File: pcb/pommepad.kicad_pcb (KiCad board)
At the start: 2 copper layers, 74.9 x 67.7 mm, 27 parts, among them SW1 SW_Push, SW2 SW_Push, SW3 SW_Push, SW4 SW_Push, SW5 SW_Push, SW6 SW_Push, U1 XIAO-RP2040-DIP, U2 OLED_0.91_128x32

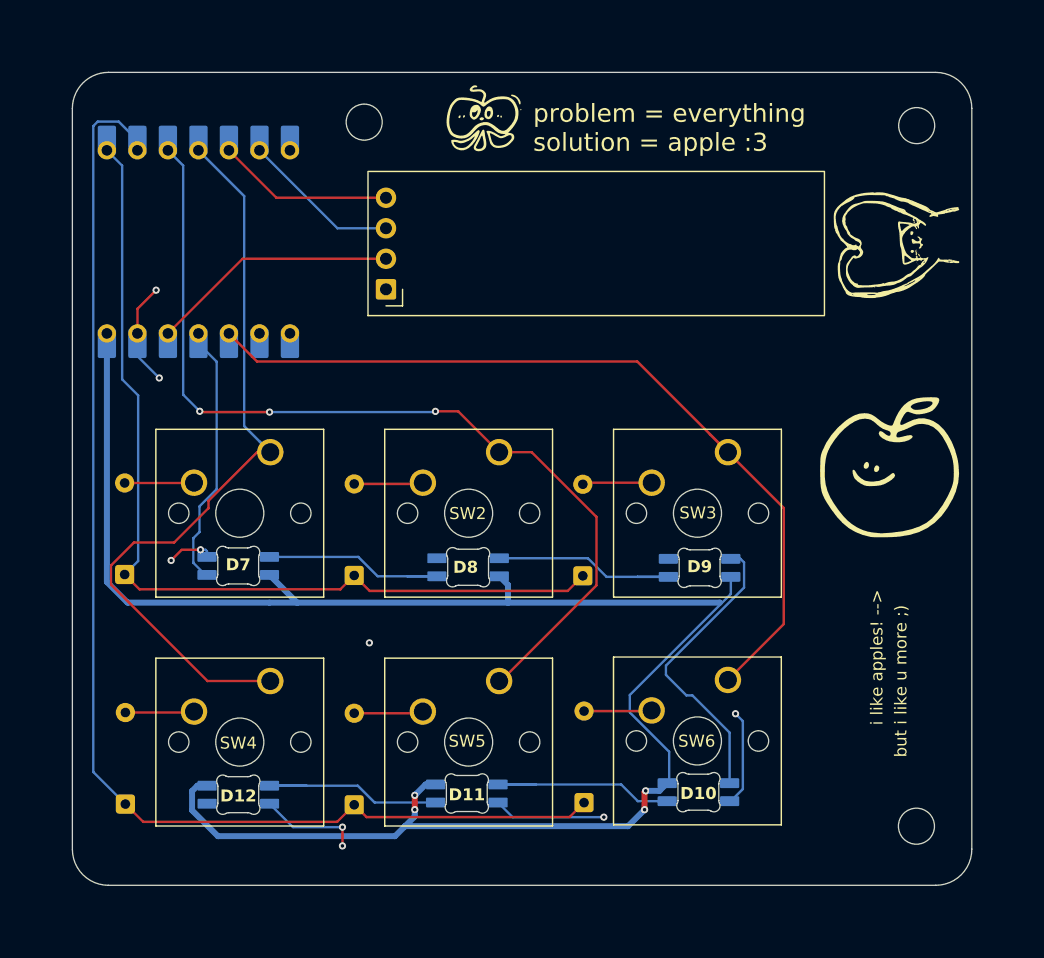
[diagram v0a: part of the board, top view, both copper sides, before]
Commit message: changing some things
changed board outline to square for easier time doing CAD, filet lines, shuffled some silkscreen around, no major changes
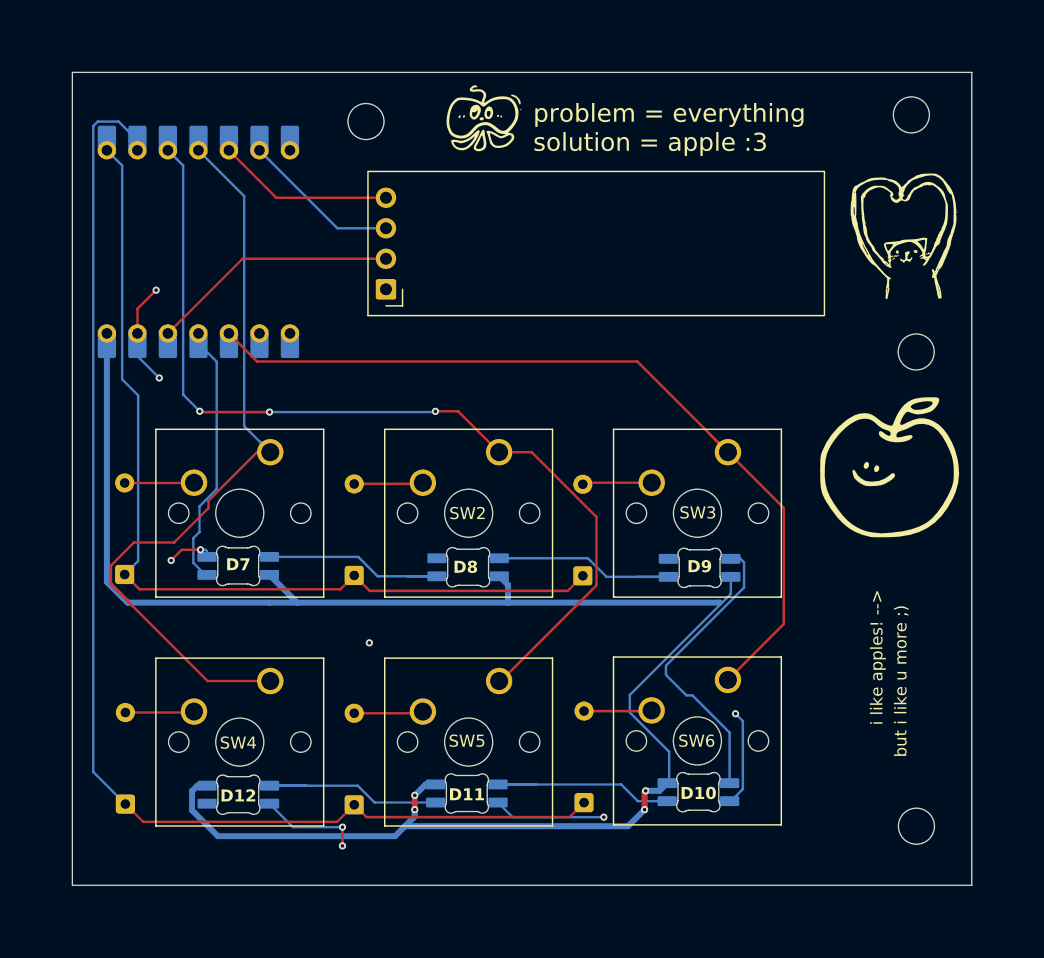
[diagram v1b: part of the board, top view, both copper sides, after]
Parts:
- added REF**: MountingHole_3mm, MountingHole:MountingHole_3mm, F.Cu at (179.9, 76.8)
- moved G*** 5.56 mm to (178.8, 63.9), turned to 0 degrees
- moved REF** 0.99 mm to (179.5, 57.1)
- moved REF** 0.16 mm to (134.1, 57.6)
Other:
- outline, holes or cut-outs redrawn

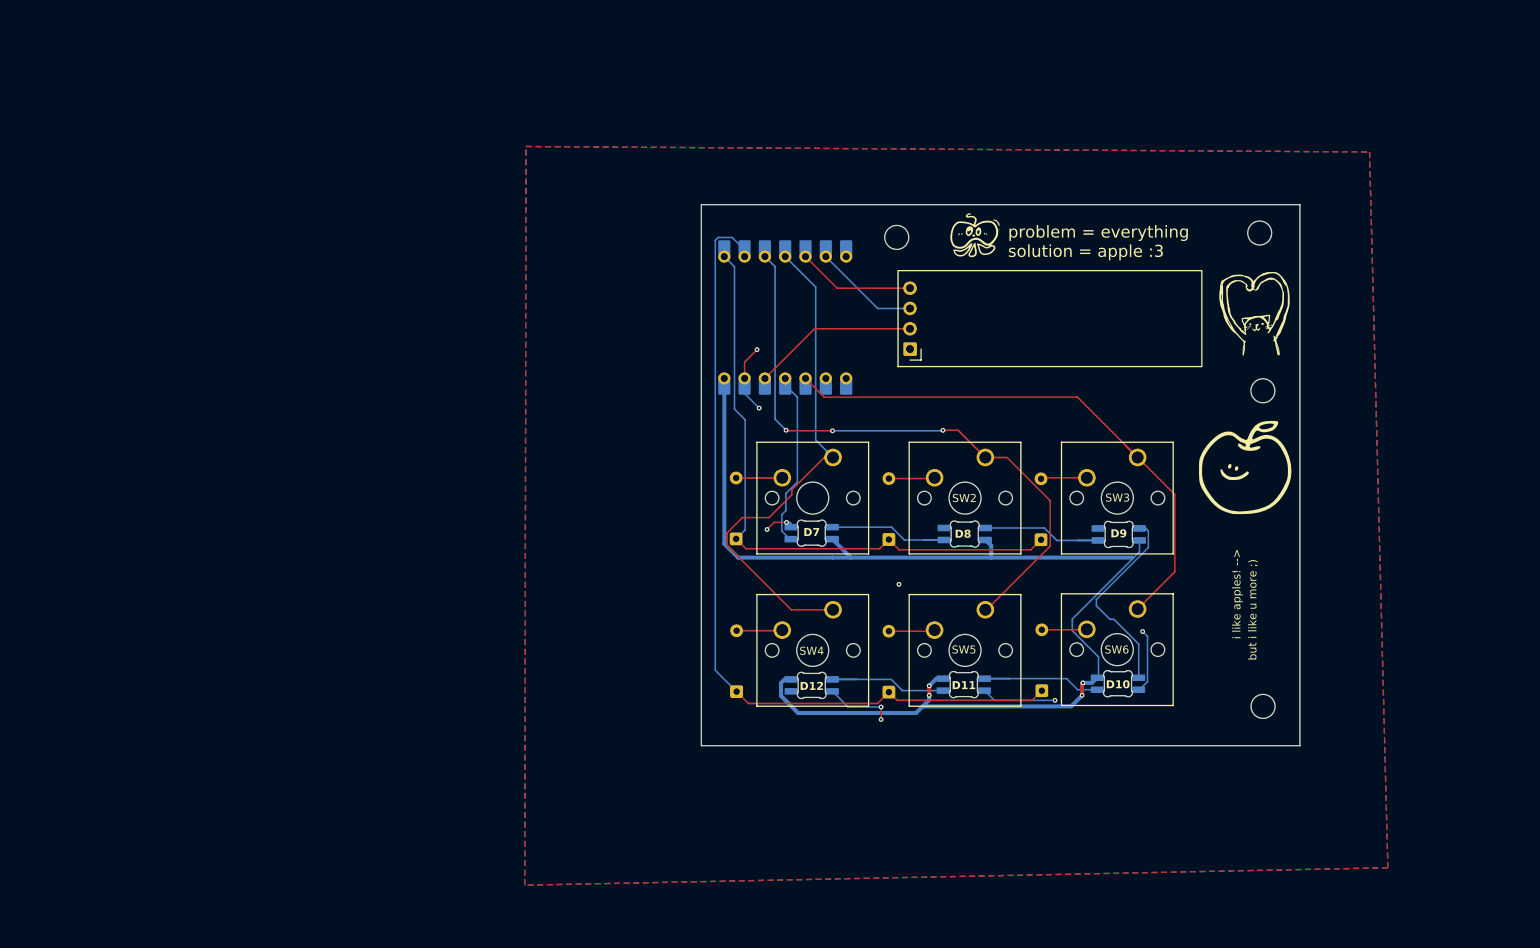
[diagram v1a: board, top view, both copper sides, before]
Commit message: done fiddling with pcb
final checks on pcb to cad, created 2 more files for gerbers and cad
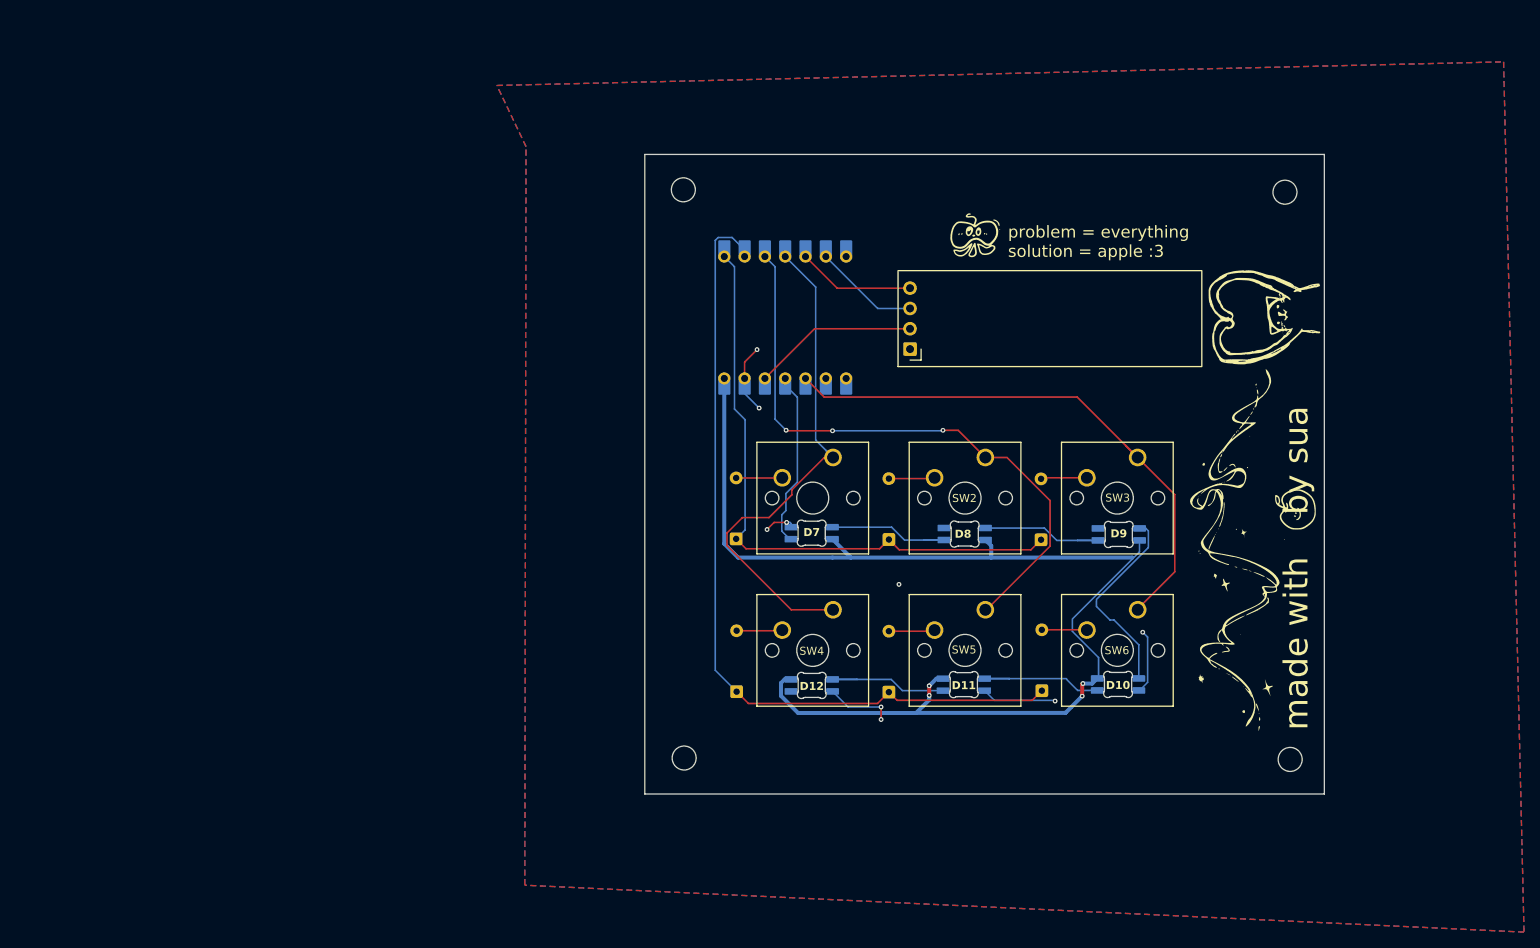
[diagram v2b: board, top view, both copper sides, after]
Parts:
- removed the G*** at (148.0, 71.7)
- removed the REF** at (179.9, 76.8)
- removed the REF** at (179.5, 57.1)
- removed the REF** at (179.9, 116.3)
- removed the REF** at (134.1, 57.6)
- added G***: LOGO, LOGO, F.Cu at (174.5, 98.7)
- added G***: LOGO, LOGO, B.Cu at (159.1, 81.4)
- added REF**: MountingHole_3mm, MountingHole:MountingHole_3mm, F.Cu at (182.7, 52.0)
- added REF**: MountingHole_3mm, MountingHole:MountingHole_3mm, F.Cu at (107.5, 122.8)
- added REF**: MountingHole_3mm, MountingHole:MountingHole_3mm, F.Cu at (183.3, 122.9)
- added REF**: MountingHole_3mm, MountingHole:MountingHole_3mm, F.Cu at (107.4, 51.7)
- moved G*** 7.86 mm to (183.9, 91.4), turned to 90 degrees
- moved G*** 4.26 mm to (176.8, 67.7), turned to 90 degrees
- moved D10 0.09 mm to (161.8, 113.6)
- moved SW6 0.09 mm to (161.7, 109.3)
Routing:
- net 5V: track 151.5 -> 152.6 mm
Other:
- board size 74.9 x 67.7 mm -> 85 x 80 mm
- board text added: "made with by sua"
- board text removed: "but i like u more ;)"
- board text removed: "i like apples! -->"
- board text removed: "看起来很简单 做起来完全不是那回事 每一步都在猜 但也走到了这里 but somehow it worked ?"
- board text removed: "苹果的糖分很高 但是它没 比你更甜哦"

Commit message: pee see bee
forgot to filet lines mb coach
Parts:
- removed the G*** at (143.9, 57.7)
- moved D10 56.4 mm to (105.5, 109.8)
- moved D8 56.4 mm to (86.3, 90.8)
- moved G*** 56.4 mm to (120.5, 63.8)
- moved REF** 56.4 mm to (127.0, 119.1)
- moved D1 56.4 mm to (57.7, 91.5)
- moved REF** 56.4 mm to (51.1, 47.8)
- moved D11 56.4 mm to (86.2, 109.8)
- moved D12 56.4 mm to (67.2, 109.9)
- moved D2 56.4 mm to (76.8, 91.6)
- moved D3 56.4 mm to (95.8, 91.6)
- moved D5 56.4 mm to (76.8, 110.6)
- moved D7 56.4 mm to (67.2, 90.7)
- moved D9 56.4 mm to (105.6, 90.8)
- moved G*** 56.4 mm to (127.6, 87.6)
- moved G*** 56.4 mm to (102.8, 77.6)
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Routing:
- net GND: vias 8 -> 9
- net (no net): vias 1 -> 0
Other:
- outline, holes or cut-outs redrawn
- board text removed: "problem = everything solution = apple :3"

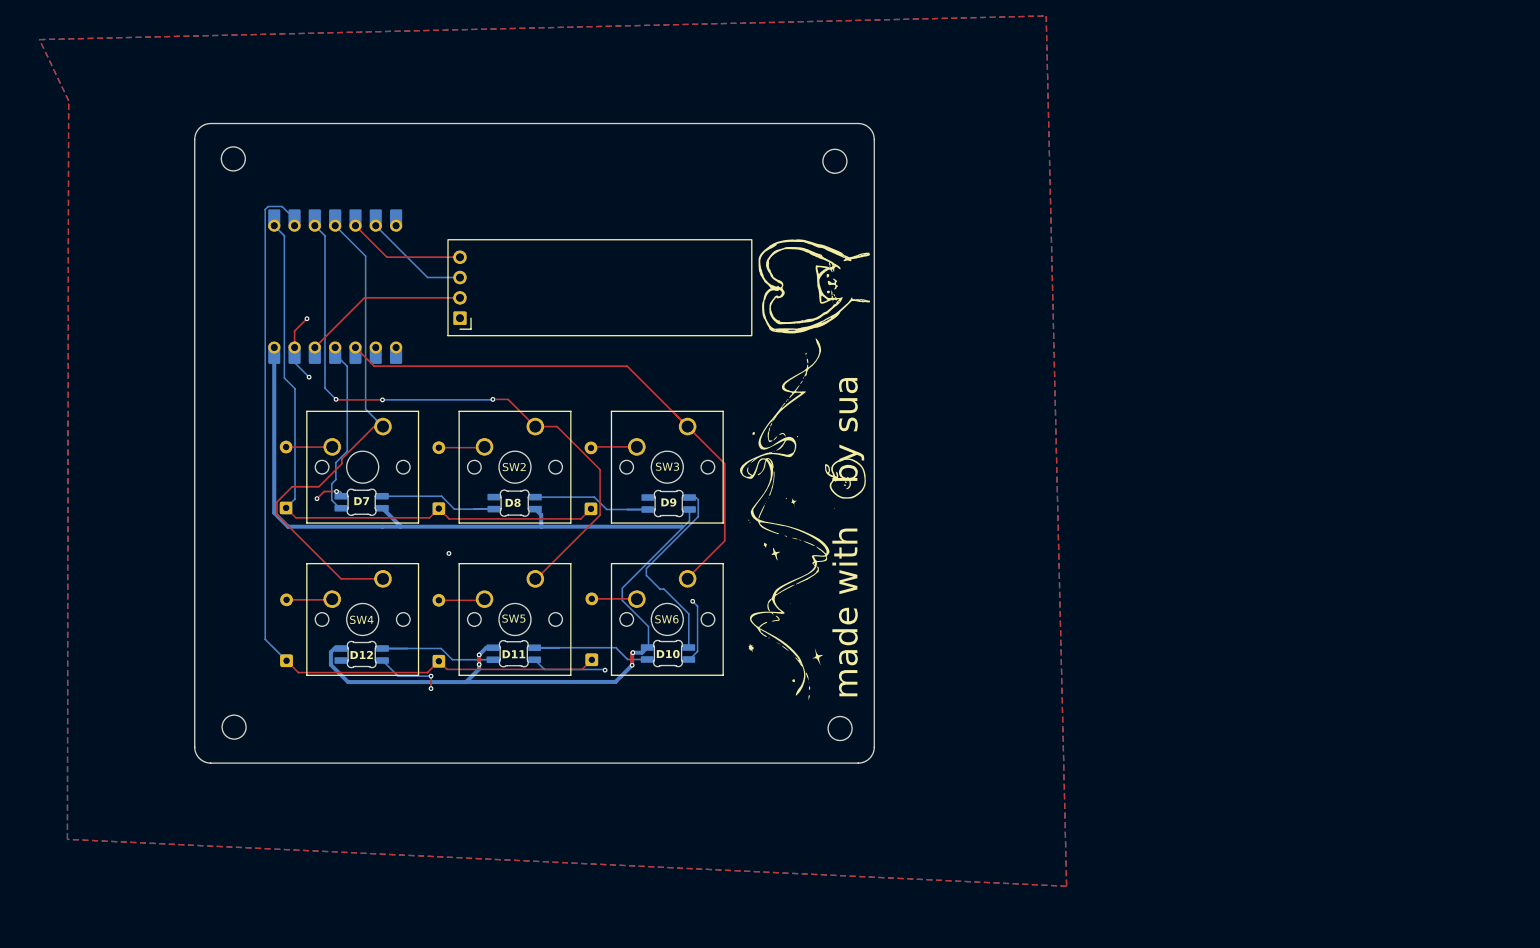
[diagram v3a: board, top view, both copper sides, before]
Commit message: edit pcb
my bad gng, changed mountin hole size and changed my board size too. 90x85, added this insanely long yap shoutout
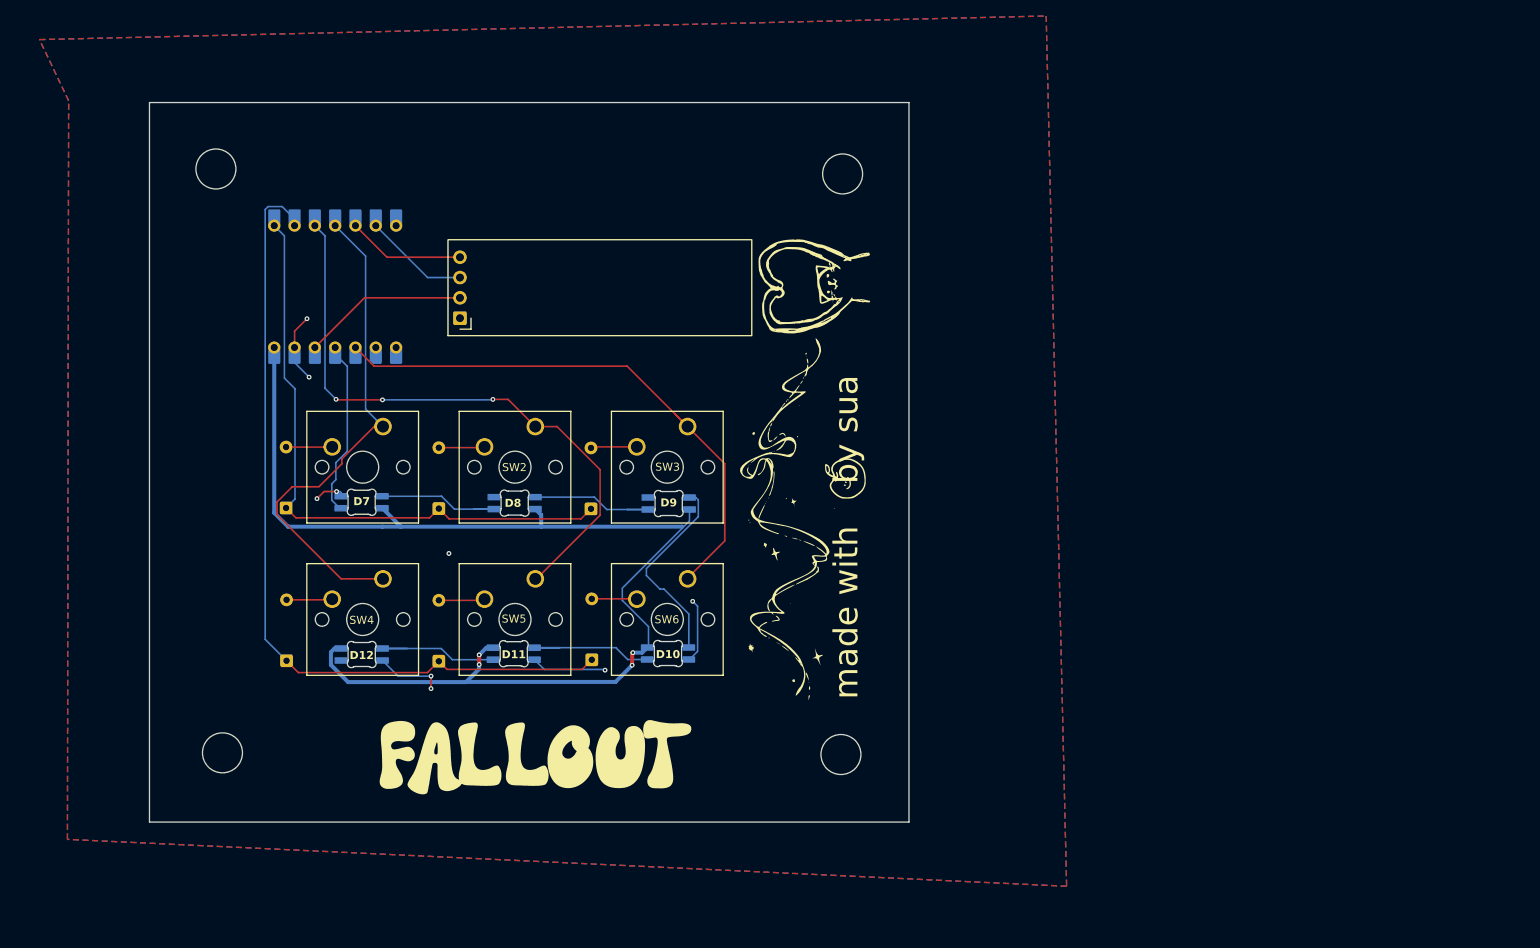
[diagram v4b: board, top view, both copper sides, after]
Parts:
- removed the REF** at (126.4, 48.1)
- removed the REF** at (51.2, 118.9)
- removed the REF** at (127.0, 119.1)
- removed the REF** at (51.1, 47.8)
- added REF**: MountingHole_5mm, MountingHole:MountingHole_5mm, F.Cu at (127.1, 122.3)
- added REF**: MountingHole_5mm, MountingHole:MountingHole_5mm, F.Cu at (49.8, 122.1)
- added REF**: MountingHole_5mm, MountingHole:MountingHole_5mm, F.Cu at (127.3, 49.7)
- added REF**: MountingHole_5mm, MountingHole:MountingHole_5mm, F.Cu at (48.9, 49.1)
- moved G*** 3.02 mm to (105.8, 77.6)
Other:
- board size 85 x 80 mm -> 95 x 90 mm
- board text added: "first of all id like to say thank you to my mom none of this would be possible without you thank you for giving birth to me okay birth okay childbirth thanks mom and thanks to my little brother who did nothing but yell at me when i was making my case and also called it ugly thanks bro. thank you to ruj who bravely stayed up past his british bedtime to britishly help me make my case and thank you 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"
